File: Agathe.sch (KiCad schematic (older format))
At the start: 173 parts, among them SW1 SW_Push, U1 ATmega32U4-AU, Y1 Crystal_GND24_Small

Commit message: Current layout before deleted keys
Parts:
- MX1, MX10, MX11, MX12, MX13, MX14, MX15, MX16, MX17, MX18, MX19, MX2, MX20, MX21, MX22, MX23, MX24, MX25, MX26, MX27, MX28, MX29, MX3, MX30, MX31, MX32, MX33, MX34, MX35, MX36, MX37, MX38, MX39, MX4, MX40, MX41, MX42, MX43, MX44, MX45, MX46, MX47, MX48, MX49, MX5, MX50, MX51, MX52, MX53, MX54, MX55, MX56, MX57, MX58, MX59, MX6, MX60, MX61, MX62, MX63, MX64, MX65, MX66, MX67, MX68, MX69, MX7, MX70, MX71, MX72, MX73, MX74, MX75, MX8, MX9: footprint MX_Only:MXOnly-1U -> MX_Only:MXOnly-1U-NoLED

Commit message: day 2 of work
MCU and USB routed
All switch routed between them
Todo: connect row and column to MCU
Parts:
- removed D44, D60, D62, D64, D67, D69, D71, D72: D_Small, Diode_SMD:D_SOD-123, symbol Device:D_Small
- removed D76, D77: 3.6V, Diode_SMD:D_SOD-123, symbol Device:D_Zener_Small
- removed MX44, MX60, MX62, MX64, MX67, MX69, MX71, MX72: MX-NoLED, MX_Only:MXOnly-1U-NoLED, symbol MX_Alps_Hybrid:MX-NoLED
- removed R7, R8: 75R, Resistor_SMD:R_0805_2012Metric, symbol Device:R_Small
- removed R9: 1.5k, Resistor_SMD:R_0805_2012Metric, symbol Device:R_Small
- added U2: PRTR5V0U2X, Package_TO_SOT_SMD:SOT-143, symbol Power_Protection:PRTR5V0U2X
- C7: footprint Diode_SMD:D_SOD-123 -> Capacitor_SMD:C_0805_2012Metric
- MX14: footprint MX_Only:MXOnly-1U-NoLED -> MX_Only:MXOnly-2U-NoLED
- MX16, MX29, MX61: footprint MX_Only:MXOnly-1U-NoLED -> MX_Only:MXOnly-1.5U-NoLED
- MX31, MX58: footprint MX_Only:MXOnly-1U-NoLED -> MX_Only:MXOnly-1.75U-NoLED
- MX43: footprint MX_Only:MXOnly-1U-NoLED -> MX_Only:MXOnly-2.25U-ReversedStabilizers-NoLED
- MX46: footprint MX_Only:MXOnly-1U-NoLED -> MX_Only:MXOnly-2.25U-NoLED
- MX63, MX66, MX70: footprint MX_Only:MXOnly-1U-NoLED -> MX_Only:MXOnly-1.25U-NoLED
- MX65: footprint MX_Only:MXOnly-1U-NoLED -> MX_Only:MXOnly-2U-ReversedStabilizers-NoLED
- MX68: footprint MX_Only:MXOnly-1U-NoLED -> MX_Only:MXOnly-2.75U-ReversedStabilizers-NoLED
- USB1: footprint Keebio-Parts:HRO-TYPE-C-31-M-12-Assembly -> Connector_USB:USB_C_Receptacle_HRO_TYPE-C-31-M-12
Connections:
- wire segments 223 -> 202
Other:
- moved on the sheet: F1

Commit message: Route everything
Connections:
- net COL0: now also U1.30 (PB6); no longer U1.26 (PD6)
- net COL1: now also U1.29 (PB5); no longer U1.27 (PD7)
- net COL10: now also U1.11 (PB3); no longer U1.29 (PB5)
- net COL11: now also U1.12 (PB7); no longer U1.28 (PB4)
- net COL14: now also U1.32 (PC7); no longer U1.11 (PB3)
- net COL2: now also U1.28 (PB4); no longer U1.1 (PE6)
- net COL3: now also U1.27 (PD7); no longer U1.32 (PC7)
- net COL4: now also U1.26 (PD6); no longer U1.31 (PC6)
- net COL5: now also U1.25 (PD4); no longer U1.30 (PB6)
- net COL6: now also U1.31 (PC6); no longer U1.25 (PD4)
- net COL7: now also U1.8 (PB0); no longer U1.9 (PB1)
- net COL8: now also U1.9 (PB1); no longer U1.8 (PB0)
- net COL9: now also U1.10 (PB2); no longer U1.12 (PB7)
- net ROW2: now also U1.22 (PD5); no longer U1.20 (PD2)
- net ROW4: now also U1.20 (PD2); no longer U1.22 (PD5)
- no-connect marks 8 -> 7
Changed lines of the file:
@@
 $EndComp
 NoConn ~ 5600 6300
+Text GLabel 2850 1850 2    50   Input ~ 0
+COL8
 Text GLabel 2850 1750 2    50   Input ~ 0
-COL8
-Text GLabel 2850 1850 2    50   Input ~ 0
 COL7
-Text GLabel 2850 2050 2    50   Input ~ 0
+Text GLabel 2850 2750 2    50   Input ~ 0
 COL14
-Text GLabel 2850 2150 2    50   Input ~ 0
-COL11
-Text GLabel 2850 2250 2    50   Input ~ 0
-COL10
-Text GLabel 2850 2350 2    50   Input ~ 0
+Text GLabel 2850 3350 2    50   Input ~ 0
 COL5
-Text GLabel 2850 2450 2    50   Input ~ 0
+Text GLabel 2850 1950 2    50   Input ~ 0
 COL9
-Text GLabel 2850 2650 2    50   Input ~ 0
+Text GLabel 2850 3550 2    50   Input ~ 0
 COL4
-Text GLabel 2850 2750 2    50   Input ~ 0
+Text GLabel 2850 3650 2    50   Input ~ 0
 COL3
 Text GLabel 2850 4150 2    50   Input ~ 0
@@
 Text GLabel 2850 4250 2    50   Input ~ 0
 ROW1
-Text GLabel 2850 3150 2    50   Input ~ 0
+Text GLabel 2850 3450 2    50   Input ~ 0
 ROW2
-Text GLabel 2850 3250 2    50   Input ~ 0
-ROW3
-Text GLabel 2850 3350 2    50   Input ~ 0
-COL6
-Text GLabel 2850 3450 2    50   Input ~ 0
-ROW4
 Text GLabel 2850 2950 2    50   Input ~ 0
 COL13
@@
 Text GLabel 2850 3050 2    50   Input ~ 0
 COL12
-Text GLabel 2850 3950 2    50   Input ~ 0
-COL2
-Text GLabel 2850 3550 2    50   Input ~ 0
+Text GLabel 2850 2350 2    50   Input ~ 0
 COL0
-Text GLabel 2850 3650 2    50   Input ~ 0
-COL1
 NoConn ~ 2850 4350
 NoConn ~ 2850 4450
@@
 NoConn ~ 2850 4650
 NoConn ~ 1650 2350
-NoConn ~ 2850 1950
 Wire Wire Line
 	10550 1800 10550 3200
@@
 	11000 3900 11000 2500
 Connection ~ 11000 2500
+Text GLabel 2850 3150 2    50   Input ~ 0
+ROW4
+Text GLabel 2850 3250 2    50   Input ~ 0
+ROW3
+Text GLabel 2850 2050 2    50   Input ~ 0
+COL10
+Text GLabel 2850 2450 2    50   Input ~ 0
+COL11
+Text GLabel 2850 2250 2    50   Input ~ 0
+COL1
+Text GLabel 2850 2150 2    50   Input ~ 0
+COL2
+Text GLabel 2850 2650 2    50   Input ~ 0
+COL6
 $EndSCHEMATC

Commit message: change the enter footprint
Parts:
- MX43: footprint MX_Only:MXOnly-2.25U-ReversedStabilizers-NoLED -> MX_Only:MXOnly-2.25U-NoLED
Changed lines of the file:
@@
 F 0 "MX43" H 9983 2773 60  0000 C CNN
 F 1 "MX-NoLED" H 9983 2699 20  0000 C CNN
-F 2 "MX_Only:MXOnly-2.25U-ReversedStabilizers-NoLED" H 9325 2525 60  0001 C CNN
+F 2 "MX_Only:MXOnly-2.25U-NoLED" H 9325 2525 60  0001 C CNN
 F 3 "" H 9325 2525 60  0001 C CNN
 	1    9950 2550

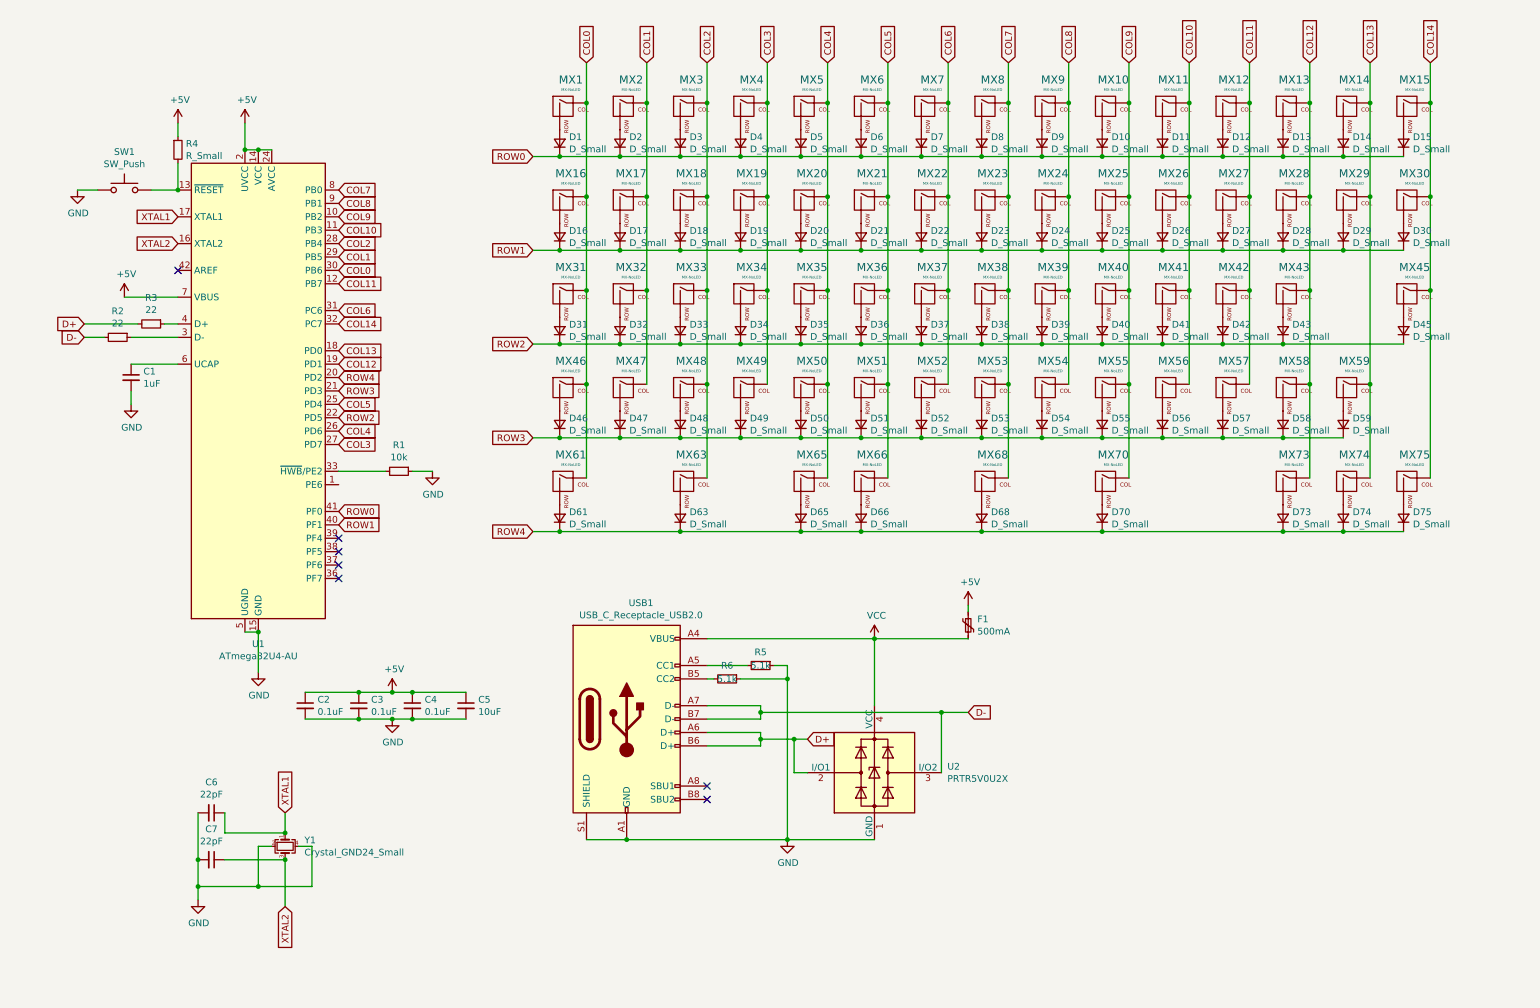
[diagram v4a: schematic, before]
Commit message: Add rotary encoder support
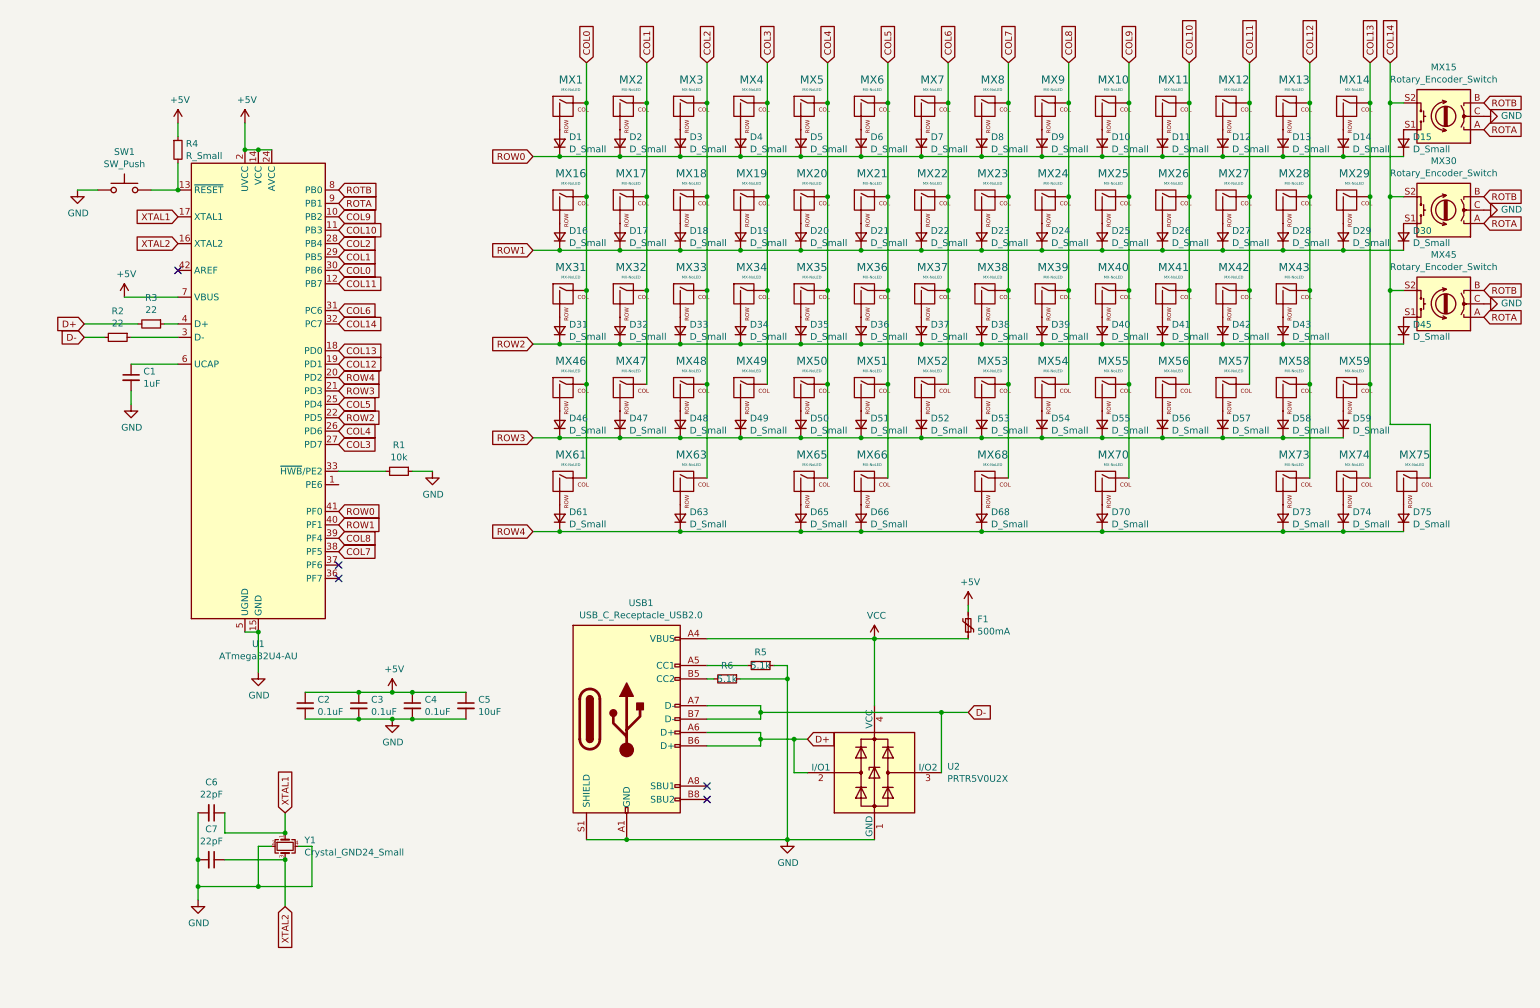
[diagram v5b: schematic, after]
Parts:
- removed MX15, MX30, MX45: MX-NoLED, MX_Only:MXOnly-1U-NoLED, symbol MX_Alps_Hybrid:MX-NoLED
- added MX15, MX30, MX45: Rotary_Encoder_Switch, Rotary_Encoder:rotary_x_MX, symbol Device:Rotary_Encoder_Switch
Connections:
- net COL14: now also MX15.S2, MX30.S2, MX45.S2
- net COL7: now also U1.38 (PF5); no longer U1.8 (PB0)
- net COL8: now also U1.39 (PF4); no longer U1.9 (PB1)
- net GND: now also MX15.C, MX30.C, MX45.C
- net at D15.2 (A): now also MX15.S1
- net at D30.2 (A): now also MX30.S1
- net at D45.2 (A): now also MX45.S1
- new net ROTA: MX15.A, MX30.A, MX45.A, U1.9 (PB1)
- new net ROTB: MX15.B, MX30.B, MX45.B, U1.8 (PB0)
- no-connect marks 7 -> 5
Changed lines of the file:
@@
-$EndComp
-$Comp
-L MX_Alps_Hybrid:MX-NoLED MX15
-U 1 1 5EB09161
-P 10850 1150
-F 0 "MX15" H 10883 1373 60  0000 C CNN
-F 1 "MX-NoLED" H 10883 1299 20  0000 C CNN
-F 2 "MX_Only:MXOnly-1U-NoLED" H 10225 1125 60  0001 C CNN
-F 3 "" H 10225 1125 60  0001 C CNN
-	1    10850 1150
-	1    0    0    -1
 $EndComp
 $Comp
@@
 $EndComp
 $Comp
-L MX_Alps_Hybrid:MX-NoLED MX30
-U 1 1 5EB1060F
-P 10850 1850
-F 0 "MX30" H 10883 2073 60  0000 C CNN
-F 1 "MX-NoLED" H 10883 1999 20  0000 C CNN
-F 2 "MX_Only:MXOnly-1U-NoLED" H 10225 1825 60  0001 C CNN
-F 3 "" H 10225 1825 60  0001 C CNN
-	1    10850 1850
-	1    0    0    -1
-$EndComp
-$Comp
 L Device:D_Small D30
 U 1 1 5EB10615
@@
 	1    9900 2800
 	0    -1   -1   0
-$EndComp
-$Comp
-L MX_Alps_Hybrid:MX-NoLED MX45
-U 1 1 5EB13C3F
-P 10850 2550
-F 0 "MX45" H 10883 2773 60  0000 C CNN
-F 1 "MX-NoLED" H 10883 2699 20  0000 C CNN
-F 2 "MX_Only:MXOnly-1U-NoLED" H 10225 2525 60  0001 C CNN
-F 3 "" H 10225 2525 60  0001 C CNN
-	1    10850 2550
-	1    0    0    -1
 $EndComp
 $Comp
@@
 Text GLabel 10550 800  1    50   Input ~ 0
 COL13
-Text GLabel 11000 800  1    50   Input ~ 0
+Text GLabel 10700 800  1    50   Input ~ 0
 COL14
 Text GLabel 4300 1500 0    50   Input ~ 0
@@
 	10550 1800 10550 1100
 Connection ~ 10550 3200
-Wire Wire Line
-	11000 800  11000 1100
-Connection ~ 11000 1100
-Wire Wire Line
-	11000 1100 11000 1800
-Connection ~ 11000 1800
-Wire Wire Line
-	11000 1800 11000 2500
 $Comp
 L MCU_Microchip_ATmega:ATmega32U4-AU U1
@@
 $EndComp
 NoConn ~ 5600 6300
-Text GLabel 2850 1850 2    50   Input ~ 0
+Text GLabel 2850 4350 2    50   Input ~ 0
 COL8
-Text GLabel 2850 1750 2    50   Input ~ 0
+Text GLabel 2850 4450 2    50   Input ~ 0
 COL7
 Text GLabel 2850 2750 2    50   Input ~ 0
@@
 Text GLabel 2850 2350 2    50   Input ~ 0
 COL0
-NoConn ~ 2850 4350
-NoConn ~ 2850 4450
 NoConn ~ 2850 4550
 NoConn ~ 2850 4650
@@
 Wire Wire Line
 	6250 5850 6350 5850
-Wire Wire Line
-	11000 3900 11000 2500
-Connection ~ 11000 2500
 Text GLabel 2850 3150 2    50   Input ~ 0
 ROW4
@@
 Text GLabel 2850 2650 2    50   Input ~ 0
 COL6
+$Comp
+L Device:Rotary_Encoder_Switch MX30
+U 1 1 5EAE26F0
+P 11100 1900
+F 0 "MX30" H 11100 1533 50  0000 C CNN
+F 1 "Rotary_Encoder_Switch" H 11100 1624 50  0000 C CNN
+F 2 "Rotary_Encoder:rotary_x_MX" H 10950 2060 50  0001 C CNN
+F 3 "~" H 11100 2160 50  0001 C CNN
+	1    11100 1900
+	-1   0    0    1
+$EndComp
+$Comp
+L Device:Rotary_Encoder_Switch MX45
+U 1 1 5EAE300D
+P 11100 2600
+F 0 "MX45" H 11100 2233 50  0000 C CNN
+F 1 "Rotary_Encoder_Switch" H 11100 2324 50  0000 C CNN
+F 2 "Rotary_Encoder:rotary_x_MX" H 10950 2760 50  0001 C CNN
+F 3 "~" H 11100 2860 50  0001 C CNN
+	1    11100 2600
+	-1   0    0    1
+$EndComp
+$Comp
+L Device:Rotary_Encoder_Switch MX15
+U 1 1 5EADE264
+P 11100 1200
+F 0 "MX15" H 11100 833 50  0000 C CNN
+F 1 "Rotary_Encoder_Switch" H 11100 924 50  0000 C CNN
+F 2 "Rotary_Encoder:rotary_x_MX" H 10950 1360 50  0001 C CNN
+F 3 "~" H 11100 1460 50  0001 C CNN
+	1    11100 1200
+	-1   0    0    1
+$EndComp
+Wire Wire Line
+	10700 800  10700 1100
+Wire Wire Line
+	10700 1100 10800 1100
+Wire Wire Line
+	10700 1100 10700 1800
+Wire Wire Line
+	10700 1800 10800 1800
+Connection ~ 10700 1100
+Wire Wire Line
+	10700 1800 10700 2500
+Wire Wire Line
+	10700 2500 10800 2500
+Connection ~ 10700 1800
+Wire Wire Line
+	10700 2500 10700 3500
+Wire Wire Line
+	10700 3500 11000 3500
+Wire Wire Line
+	11000 3500 11000 3900
+Connection ~ 10700 2500
+$Comp
+L power:GND #PWR0113
+U 1 1 5EBCE257
+P 11400 1200
+F 0 "#PWR0113" H 11400 950 50  0001 C CNN
+F 1 "GND" V 11405 1072 50  0000 R CNN
+F 2 "" H 11400 1200 50  0001 C CNN
+F 3 "" H 11400 1200 50  0001 C CNN
+	1    11400 1200
+	0    -1   -1   0
+$EndComp
+$Comp
+L power:GND #PWR0115
+U 1 1 5EBCE8DB
+P 11400 1900
+F 0 "#PWR0115" H 11400 1650 50  0001 C CNN
+F 1 "GND" V 11405 1772 50  0000 R CNN
+F 2 "" H 11400 1900 50  0001 C CNN
+F 3 "" H 11400 1900 50  0001 C CNN
+	1    11400 1900
+	0    -1   -1   0
+$EndComp
+$Comp
+L power:GND #PWR0116
+U 1 1 5EBCEE25
+P 11400 2600
+F 0 "#PWR0116" H 11400 2350 50  0001 C CNN
+F 1 "GND" V 11405 2472 50  0000 R CNN
+F 2 "" H 11400 2600 50  0001 C CNN
+F 3 "" H 11400 2600 50  0001 C CNN
+	1    11400 2600
+	0    -1   -1   0
+$EndComp
+Text GLabel 11400 1300 2    50   Input ~ 0
+ROTA
+Text GLabel 11400 1100 2    50   Input ~ 0
+ROTB
+Text GLabel 11400 2000 2    50   Input ~ 0
+ROTA
+Text GLabel 11400 2700 2    50   Input ~ 0
+ROTA
+Text GLabel 11400 1800 2    50   Input ~ 0
+ROTB
+Text GLabel 11400 2500 2    50   Input ~ 0
+ROTB
+Text GLabel 2850 1850 2    50   Input ~ 0
+ROTA
+Text GLabel 2850 1750 2    50   Input ~ 0
+ROTB
 $EndSCHEMATC

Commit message: Add underglow
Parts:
- added LED1, LED10, LED11, LED12, LED13, LED14, LED15, LED16, LED2, LED3, LED4, LED5, LED6, LED7, LED8, LED9: WS2812B, LED_SMD:LED_WS2812B_PLCC4_5.0x5.0mm_P3.2mm, symbol LED:WS2812B
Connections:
- net +5V: now also LED1.3 (VSS), LED10.3 (VSS), LED11.3 (VSS), LED12.3 (VSS), LED13.3 (VSS), LED14.3 (VSS), LED15.3 (VSS), LED16.3 (VSS), LED2.3 (VSS), LED3.3 (VSS), LED4.3 (VSS), LED5.3 (VSS), LED6.3 (VSS), LED7.3 (VSS), LED8.3 (VSS), LED9.3 (VSS)
- net COL0: now also U1.31 (PC6); no longer U1.30 (PB6)
- net COL6: now also U1.36 (PF7); no longer U1.31 (PC6)
- net GND: now also LED1.1 (VDD), LED10.1 (VDD), LED11.1 (VDD), LED12.1 (VDD), LED13.1 (VDD), LED14.1 (VDD), LED15.1 (VDD), LED16.1 (VDD), LED2.1 (VDD), LED3.1 (VDD), LED4.1 (VDD), LED5.1 (VDD), LED6.1 (VDD), LED7.1 (VDD), LED8.1 (VDD), LED9.1 (VDD)
- new net: LED2.2 (DOUT), LED3.4 (DIN)
- new net: LED1.2 (DOUT), LED2.4 (DIN)
- new net: LED3.2 (DOUT), LED4.4 (DIN)
- new net: LED4.2 (DOUT), LED5.4 (DIN)
- new net: LED5.2 (DOUT), LED6.4 (DIN)
- new net: LED6.2 (DOUT), LED7.4 (DIN)
- new net: LED7.2 (DOUT), LED8.4 (DIN)
- new net: LED8.2 (DOUT), LED9.4 (DIN)
- new net: LED10.4 (DIN), LED9.2 (DOUT)
- new net: LED10.2 (DOUT), LED11.4 (DIN)
- new net: LED11.2 (DOUT), LED12.4 (DIN)
- new net: LED12.2 (DOUT), LED13.4 (DIN)
- new net: LED13.2 (DOUT), LED14.4 (DIN)
- new net: LED14.2 (DOUT), LED15.4 (DIN)
- new net: LED15.2 (DOUT), LED16.4 (DIN)
- new net LED: LED1.4 (DIN), U1.30 (PB6)
- no-connect marks 5 -> 6
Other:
- moved on the sheet: C1, C2, C3, C4, C5, C6, C7, D1, D10, D11, D12, D13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

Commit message: Update footprints for switch
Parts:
- MX1, MX10, MX11, MX12, MX13, MX17, MX18, MX19, MX2, MX20, MX21, MX22, MX23, MX24, MX25, MX26, MX27, MX28, MX3, MX32, MX33, MX34, MX35, MX36, MX37, MX38, MX39, MX4, MX40, MX41, MX42, MX47, MX48, MX49, MX5, MX50, MX51, MX52, MX53, MX54, MX55, MX56, MX57, MX59, MX6, MX7, MX73, MX74, MX75, MX8, MX9: footprint MX_Only:MXOnly-1U-NoLED -> parts:mx_1u
- MX14: footprint MX_Only:MXOnly-2U-NoLED -> parts:mx_2u
- MX16, MX29, MX61: footprint MX_Only:MXOnly-1.5U-NoLED -> parts:mx_15u
- MX31, MX58: footprint MX_Only:MXOnly-1.75U-NoLED -> parts:mx_175u
- MX43, MX46: footprint MX_Only:MXOnly-2.25U-NoLED -> parts:mx_225u
- MX63, MX66, MX70: footprint MX_Only:MXOnly-1.25U-NoLED -> parts:mx_125u
- MX65: footprint MX_Only:MXOnly-2U-ReversedStabilizers-NoLED -> parts:mx_2ureverse
- MX68: footprint MX_Only:MXOnly-2.75U-ReversedStabilizers-NoLED -> parts:mx_275u_reverse

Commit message: add 2 breakout header for VCC and GND (#8)
* Add submodule explanation

* add render view

* Rerouting around USB-C connector

* WIP

* end

* end

* add 2 breakout header for VCC and GND
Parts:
- added J1: Conn_01x04_Female, Connector_PinHeader_2.54mm:PinHeader_1x04_P2.54mm_Vertical, symbol Connector:Conn_01x04_Female
- added J2: GPIO 1, Connector_PinHeader_2.54mm:PinHeader_1x01_P2.54mm_Vertical, symbol Connector:Conn_01x01_Female
- added J3: GPIO 2, Connector_PinHeader_2.54mm:PinHeader_1x01_P2.54mm_Vertical, symbol Connector:Conn_01x01_Female
- added J4: Conn_01x02_Female, Connector_PinHeader_2.54mm:PinHeader_1x02_P2.54mm_Vertical, symbol Connector:Conn_01x02_Female
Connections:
- net D+: now also J1.2 (Pin_2)
- net D-: now also J1.3 (Pin_3)
- net GND: now also J1.4 (Pin_4), J4.2 (Pin_2)
- net VCC: now also J1.1 (Pin_1), J4.1 (Pin_1)
- net at U1.1 (PE6): now also J2.1 (Pin_1)
- net at U1.37 (PF6): now also J3.1 (Pin_1)
- no-connect marks 6 -> 4
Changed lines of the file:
@@
 Text GLabel 2550 2500 2    50   Input ~ 0
 COL12
-NoConn ~ 2550 4000
 NoConn ~ 1350 1800
 Wire Wire Line
@@
 	4800 5750 4500 5750
 NoConn ~ 3900 5750
-NoConn ~ 2550 3400
 Text GLabel 2550 2100 2    50   Input ~ 0
 COL0
@@
 $EndComp
 Connection ~ 4200 5200
+$Comp
+L Connector:Conn_01x04_Female J1
+U 1 1 5F7DB4E9
+P 6050 6700
+F 0 "J1" H 6078 6676 50  0000 L CNN
+F 1 "Conn_01x04_Female" H 6078 6585 50  0000 L CNN
+F 2 "Connector_PinHeader_2.54mm:PinHeader_1x04_P2.54mm_Vertical" H 6050 6700 50  0001 C CNN
+F 3 "~" H 6050 6700 50  0001 C CNN
+	1    6050 6700
+	1    0    0    -1
+$EndComp
+Text GLabel 5800 6800 0    50   Input ~ 0
+D-
+Text GLabel 5800 6700 0    50   Input ~ 0
+D+
+Wire Wire Line
+	5850 6600 5800 6600
+Wire Wire Line
+	5850 6700 5800 6700
+Wire Wire Line
+	5850 6800 5800 6800
+Wire Wire Line
+	5800 6900 5850 6900
+$Comp
+L power:GND #PWR02
+U 1 1 5F8431E2
+P 5800 6900
+F 0 "#PWR02" H 5800 6650 50  0001 C CNN
+F 1 "GND" H 5805 6727 50  0000 C CNN
+F 2 "" H 5800 6900 50  0001 C CNN
+F 3 "" H 5800 6900 50  0001 C CNN
+	1    5800 6900
+	1    0    0    -1
+$EndComp
+$Comp
+L power:VCC #PWR01
+U 1 1 5F84490E
+P 5800 6600
+F 0 "#PWR01" H 5800 6450 50  0001 C CNN
+F 1 "VCC" H 5815 6773 50  0000 C CNN
+F 2 "" H 5800 6600 50  0001 C CNN
+F 3 "" H 5800 6600 50  0001 C CNN
+	1    5800 6600
+	1    0    0    -1
+$EndComp
+$Comp
+L Connector:Conn_01x01_Female J2
+U 1 1 5F7E232B
+P 2750 3400
+F 0 "J2" H 2778 3426 50  0000 L CNN
+F 1 "GPIO 1" H 2778 3335 50  0000 L CNN
+F 2 "Connector_PinHeader_2.54mm:PinHeader_1x01_P2.54mm_Vertical" H 2750 3400 50  0001 C CNN
+F 3 "~" H 2750 3400 50  0001 C CNN
+	1    2750 3400
+	1    0    0    -1
+$EndComp
+$Comp
+L Connector:Conn_01x01_Female J3
+U 1 1 5F7E3E80
+P 2750 4000
+F 0 "J3" H 2778 4026 50  0000 L CNN
+F 1 "GPIO 2" H 2778 3935 50  0000 L CNN
+F 2 "Connector_PinHeader_2.54mm:PinHeader_1x01_P2.54mm_Vertical" H 2750 4000 50  0001 C CNN
+F 3 "~" H 2750 4000 50  0001 C CNN
+	1    2750 4000
+	1    0    0    -1
+$EndComp
+$Comp
+L Connector:Conn_01x02_Female J4
+U 1 1 5F803717
+P 4850 6600
+F 0 "J4" H 4878 6576 50  0000 L CNN
+F 1 "Conn_01x02_Female" H 4878 6485 50  0000 L CNN
+F 2 "Connector_PinHeader_2.54mm:PinHeader_1x02_P2.54mm_Vertical" H 4850 6600 50  0001 C CNN
+F 3 "~" H 4850 6600 50  0001 C CNN
+	1    4850 6600
+	1    0    0    -1
+$EndComp
+$Comp
+L power:VCC #PWR03
+U 1 1 5F805F11
+P 4650 6600
+F 0 "#PWR03" H 4650 6450 50  0001 C CNN
+F 1 "VCC" H 4665 6773 50  0000 C CNN
+F 2 "" H 4650 6600 50  0001 C CNN
+F 3 "" H 4650 6600 50  0001 C CNN
+	1    4650 6600
+	1    0    0    -1
+$EndComp
+$Comp
+L power:GND #PWR04
+U 1 1 5F807ABA
+P 4650 6700
+F 0 "#PWR04" H 4650 6450 50  0001 C CNN
+F 1 "GND" H 4655 6527 50  0000 C CNN
+F 2 "" H 4650 6700 50  0001 C CNN
+F 3 "" H 4650 6700 50  0001 C CNN
+	1    4650 6700
+	1    0    0    -1
+$EndComp
 $EndSCHEMATC
